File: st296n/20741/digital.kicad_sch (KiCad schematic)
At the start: 61 parts, among them J2 ID, Q14 "1A", U1 8051, U13 74LS155, U2 74LS573, U21 74LS174, U22 74LS174, U23 74LS174, U24 74LS257, U27 74LS00, U28 74LS196, U29 74LS123, U3 74LS14, U30 74F08, U4 CDM6264, U9 11741-502, Y1 10MHz, Y2 20MHz

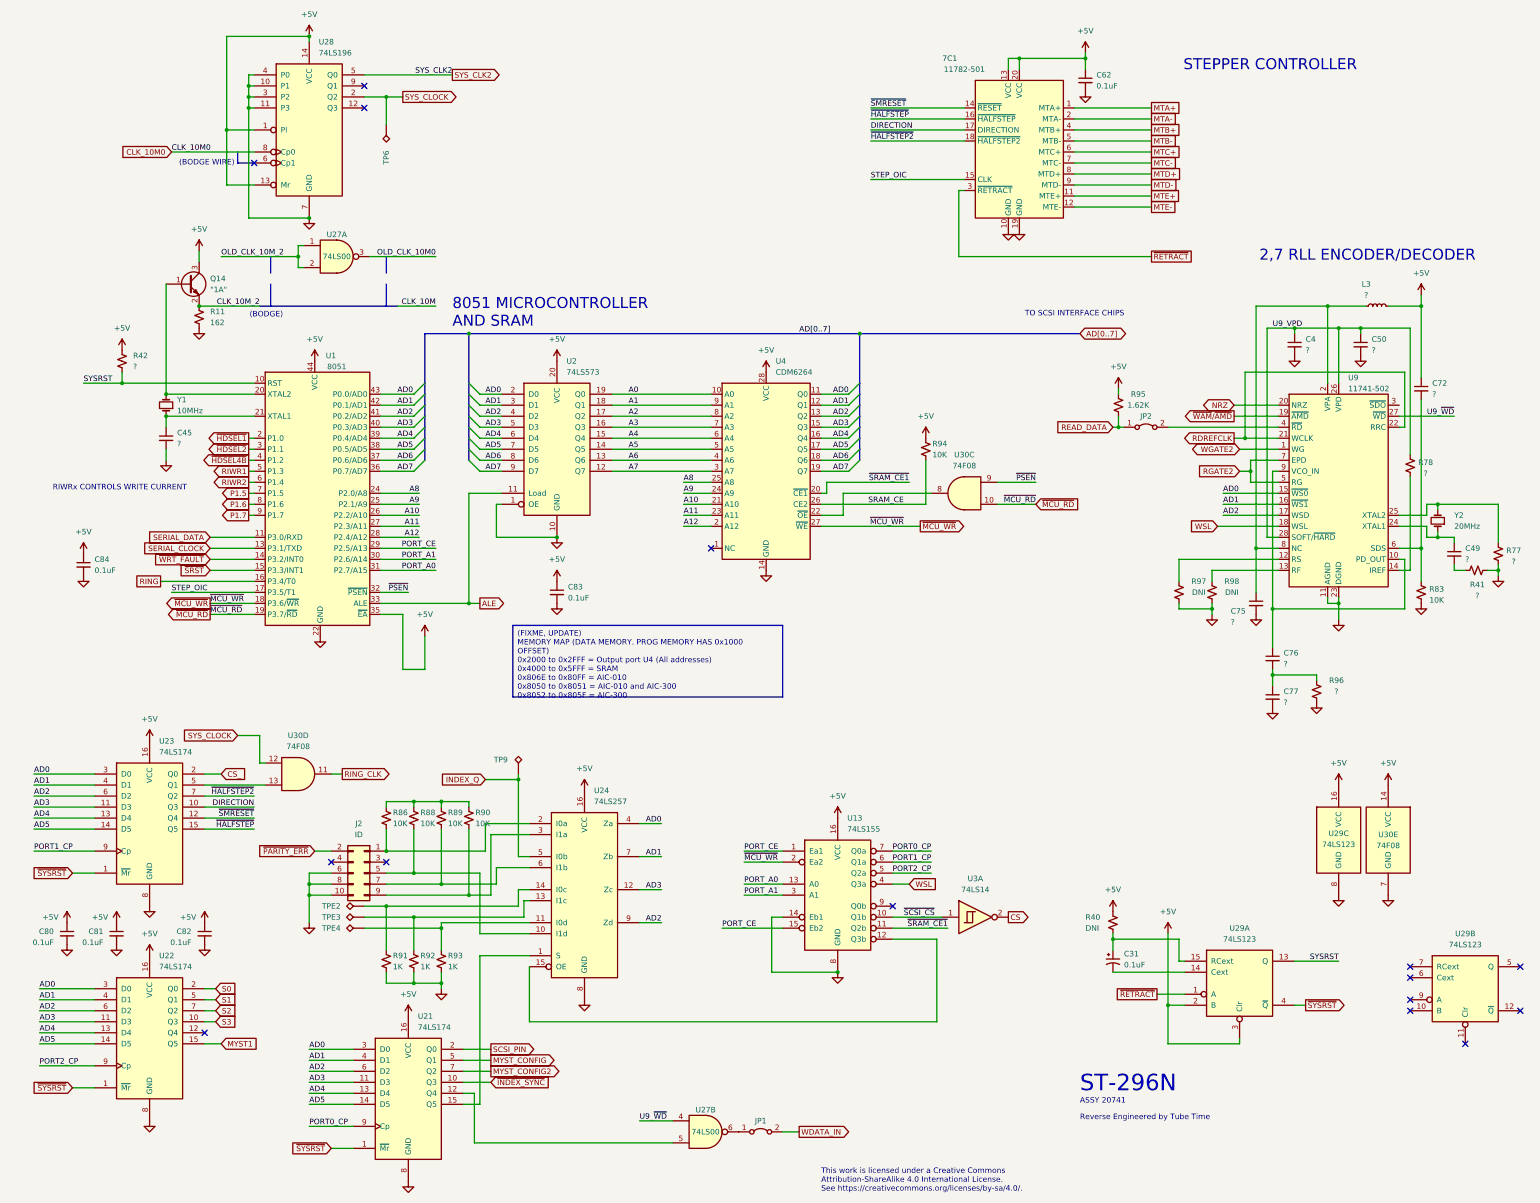
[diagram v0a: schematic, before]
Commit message: st296n fix passives
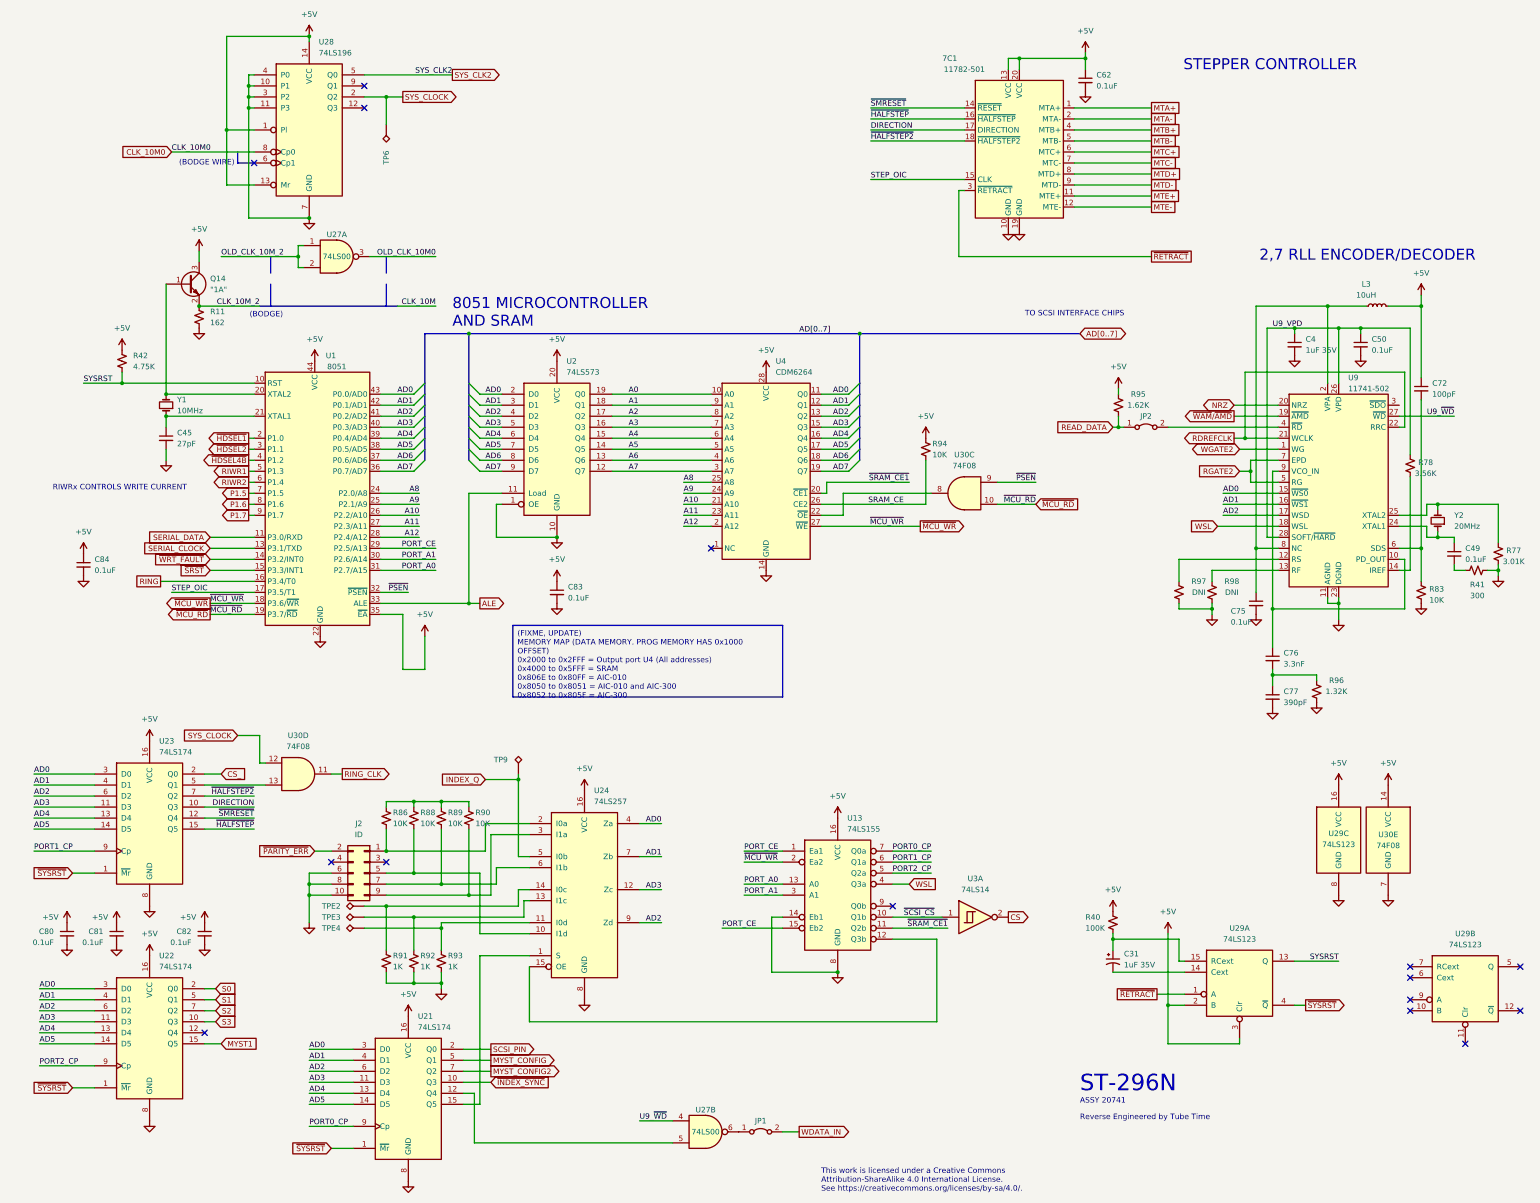
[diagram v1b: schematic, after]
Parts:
- C31: value 0.1uF -> 1uF 35V
- C4: value ? -> 1uF 35V
- C45: value ? -> 27pF
- C49, C50, C75: value ? -> 0.1uF
- C72: value ? -> 100pF
- C76: value ? -> 3.3nF
- C77: value ? -> 390pF
- L3: value ? -> 10uH
- R40: value DNI -> 100K
- R41: value ? -> 300
- R42: value ? -> 4.75K
- R77: value ? -> 3.01K
- R78: value ? -> 3.56K
- R96: value ? -> 1.32K
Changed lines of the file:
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@@
 			)
 		)
-		(property "Value" "?"
+		(property "Value" "4.75K"
 			(at 83.82 92.7099 0)
 			(effects
@@
 		(fields_autoplaced yes)
 		(property "Reference" "C31"
-			(at 312.42 228.1682 0)
+			(at 312.42 228.1681 0)
 			(effects
 				(font
@@
 			)
 		)
-		(property "Value" "0.1uF"
-			(at 312.42 230.7082 0)
+		(property "Value" "1uF 35V"
+			(at 312.42 230.7081 0)
 			(effects
 				(font
@@
 			)
 		)
-		(property "Value" "?"
+		(property "Value" "300"
 			(at 393.954 145.542 90)
 			(effects
@@
 			)
 		)
-		(property "Value" "?"
+		(property "Value" "3.56K"
 			(at 382.016 117.348 0)
 			(effects
@@
 			)
 		)
-		(property "Value" "?"
+		(property "Value" "0.1uF"
 			(at 391.16 137.1662 0)
 			(effects
@@
 			)
 		)
-		(property "Value" "?"
+		(property "Value" "0.1uF"
 			(at 337.058 151.638 0)
 			(effects
@@
 			)
 		)
-		(property "Value" "?"
+		(property "Value" "3.01K"
 			(at 402.336 137.668 0)
 			(effects
@@
 			)
 		)
-		(property "Value" "?"
+		(property "Value" "390pF"
 			(at 349.25 170.1862 0)
 			(effects
@@
 			)
 		)
-		(property "Value" "?"
+		(property "Value" "1.32K"
 			(at 361.442 167.64 0)
 			(effects
@@
 			)
 		)
-		(property "Value" "?"
+		(property "Value" "0.1uF"
 			(at 369.57 88.9062 0)
 			(effects
@@
 			)
 		)
-		(property "Value" "?"
+		(property "Value" "3.3nF"
 			(at 349.25 161.2962 0)
 			(effects
@@
 			)
 		)
-		(property "Value" "?"
+		(property "Value" "100pF"
 			(at 383.54 99.0662 0)
 			(effects
@@
 			)
 		)
-		(property "Value" "?"
+		(property "Value" "10uH"
 			(at 368.3 76.2 90)
 			(effects
@@
 			)
 		)
-		(property "Value" "?"
+		(property "Value" "1uF 35V"
 			(at 354.33 88.9062 0)
 			(effects
@@
 			)
 		)
-		(property "Value" "?"
+		(property "Value" "27pF"
 			(at 93.98 110.4962 0)
 			(effects
@@
 			)
 		)
-		(property "Value" "DNI"
+		(property "Value" "100K"
 			(at 303.53 222.25 0)
 			(effects

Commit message: st296n update symbol with more chip info
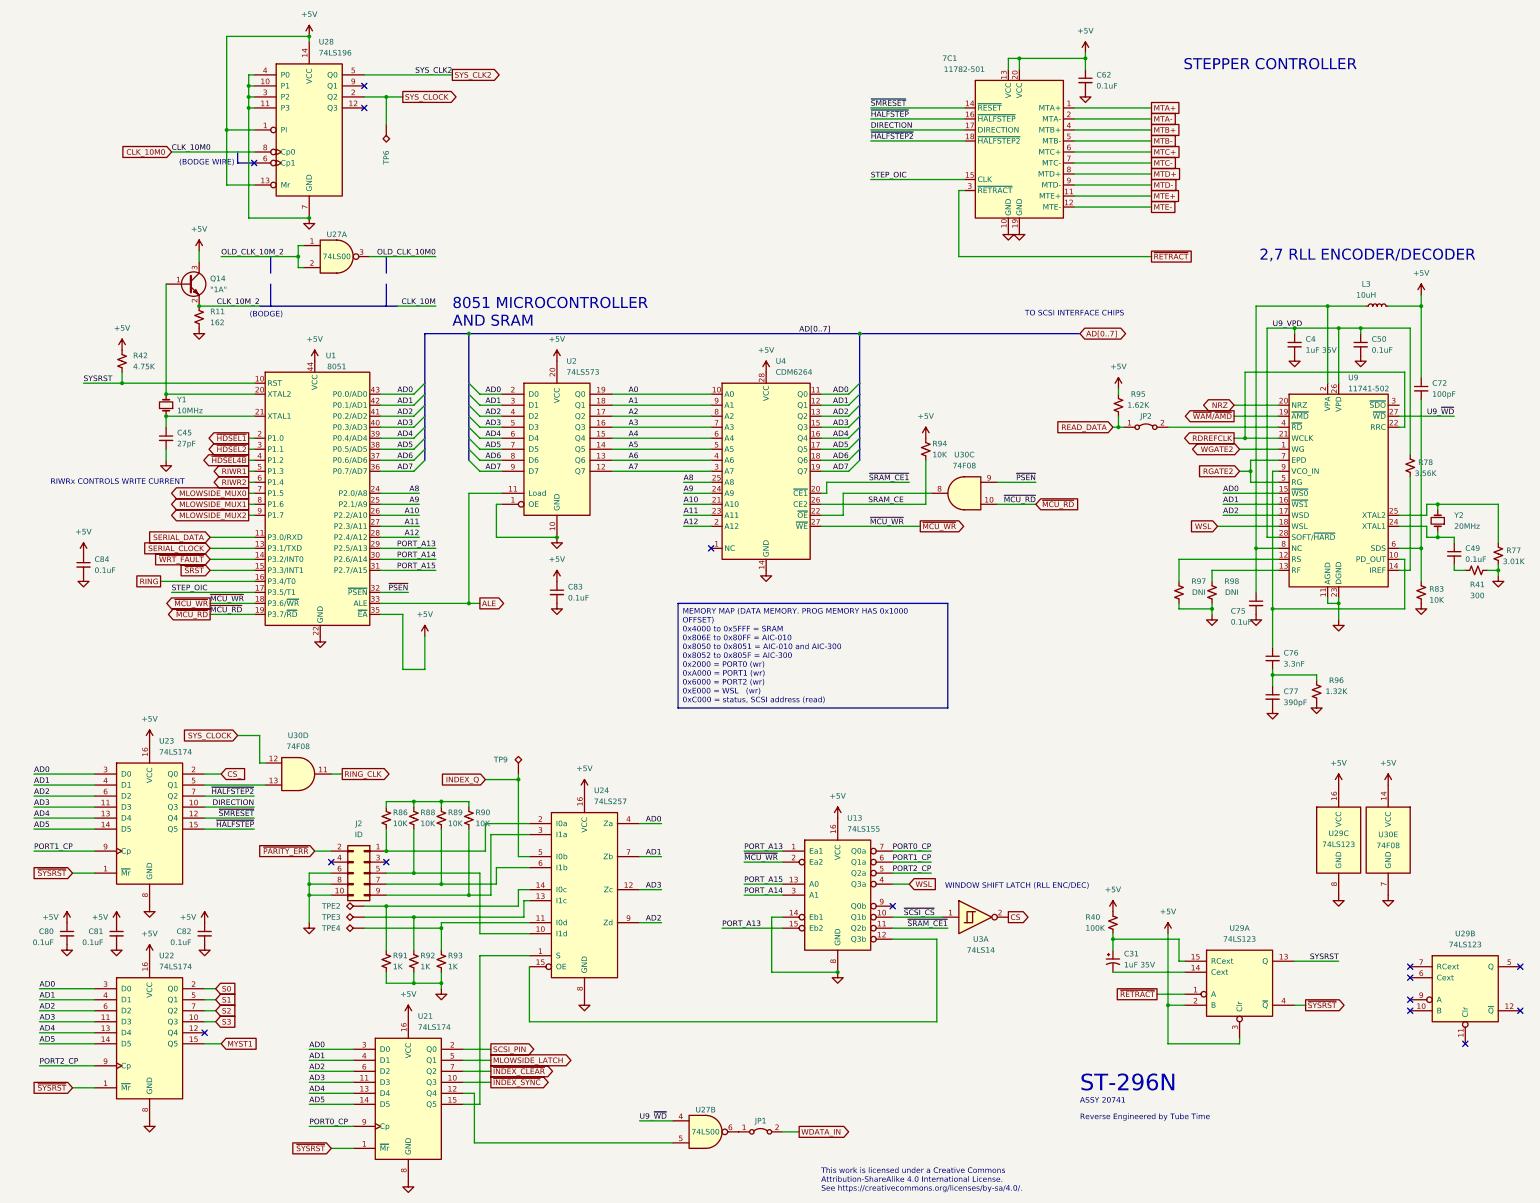
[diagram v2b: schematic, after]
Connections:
- net MYST_CONFIG renamed MLOWSIDE_LATCH
- net MYST_CONFIG2 renamed ~{INDEX_CLEAR}
- net P1.5 renamed MLOWSIDE_MUX0
- net P1.6 renamed MLOWSIDE_MUX1
- net P1.7 renamed MLOWSIDE_MUX2
- net PORT_A0 renamed PORT_A15
- net PORT_A1 renamed PORT_A14
- net PORT_CE renamed PORT_A13
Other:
- note added: "WINDOW SHIFT LATCH (RLL ENC/DEC)"
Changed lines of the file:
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@@
 		)
 	)
-	(text_box "(FIXME, UPDATE)\nMEMORY MAP (DATA MEMORY. PROG MEMORY HAS 0x1000 OFFSET)\n0x2000 to 0x2FFF = Output port U4 (All addresses)\n0x4000 to 0x5FFF = SRAM\n0x806E to 0x80FF = AIC-010\n0x8050 to 0x8051 = AIC-010 and AIC-300\n0x8052 to 0x805F = AIC-300"
+	(text_box "MEMORY MAP (DATA MEMORY. PROG MEMORY HAS 0x1000 OFFSET)\n0x4000 to 0x5FFF = SRAM\n0x806E to 0x80FF = AIC-010\n0x8050 to 0x8051 = AIC-010 and AIC-300\n0x8052 to 0x805F = AIC-300\n0x2000 = PORT0 (wr)\n0xA000 = PORT1 (wr)\n0x6000 = PORT2 (wr)\n0xE000 = WSL   (wr)\n0xC000 = status, SCSI address (read)\n\n"
 		(exclude_from_sim no)
-		(at 171.45 152.4 0)
-		(size 62.23 16.51)
+		(at 209.55 147.32 0)
+		(size 62.23 24.13)
 		(stroke
 			(width 0)
@@
 		)
 	)
+	(text "WINDOW SHIFT LATCH (RLL ENC/DEC)"
+		(exclude_from_sim no)
+		(at 287.782 212.598 0)
+		(effects
+			(font
+				(size 1.27 1.27)
+			)
+		)
+	)
 	(text "8051 MICROCONTROLLER\nAND SRAM"
 		(exclude_from_sim no)
@@
 	(text "RIWRx CONTROLS WRITE CURRENT"
 		(exclude_from_sim no)
-		(at 65.278 121.412 0)
+		(at 64.77 120.142 0)
 		(effects
 			(font
@@
 		)
 	)
-	(label "PORT_CE"
+	(label "PORT_A13"
 		(at 153.67 134.62 180)
 		(fields_autoplaced yes)
@@
 		)
 	)
-	(label "PORT_A0"
+	(label "PORT_A15"
 		(at 153.67 139.7 180)
 		(fields_autoplaced yes)
@@
 		)
 	)
-	(label "PORT_A1"
+	(label "PORT_A14"
 		(at 153.67 137.16 180)
 		(fields_autoplaced yes)
@@
 		)
 	)
-	(label "PORT_CE"
+	(label "PORT_A13"
 		(at 224.79 204.47 0)
 		(fields_autoplaced yes)
@@
 		)
 	)
-	(label "PORT_A0"
+	(label "PORT_A15"
 		(at 224.79 212.09 0)
 		(fields_autoplaced yes)
@@
 		)
 	)
-	(label "PORT_A1"
+	(label "PORT_A14"
 		(at 224.79 214.63 0)
 		(fields_autoplaced yes)
@@
 		)
 	)
-	(label "PORT_CE"
+	(label "PORT_A13"
 		(at 219.71 222.25 0)
 		(fields_autoplaced yes)
@@
 		)
 	)
-	(global_label "P1.6"
+	(global_label "MLOWSIDE_MUX1"
 		(shape output)
 		(at 110.49 124.46 180)
@@
 		)
 	)
-	(global_label "P1.7"
+	(global_label "MLOWSIDE_MUX2"
 		(shape output)
 		(at 110.49 127 180)
@@
 		)
 	)
-	(global_label "MYST_CONFIG2"
+	(global_label "~{INDEX_CLEAR}"
 		(shape output)
 		(at 166.37 255.27 0)
@@
 		)
 	)
-	(global_label "MYST_CONFIG"
+	(global_label "MLOWSIDE_LATCH"
 		(shape output)
 		(at 166.37 252.73 0)
@@
 	)
 	(global_label "~{INDEX_SYNC}"
-		(shape input)
+		(shape output)
 		(at 166.37 257.81 0)
 		(fields_autoplaced yes)
@@
 		)
 	)
-	(global_label "P1.5"
+	(global_label "MLOWSIDE_MUX0"
 		(shape output)
 		(at 110.49 121.92 180)
@@
 		(on_board yes)
 		(dnp no)
-		(fields_autoplaced yes)
 		(property "Reference" "U3"
-			(at 278.13 210.82 0)
+			(at 279.4 224.79 0)
 			(effects
 				(font
@@
 		)
 		(property "Value" "74LS14"
-			(at 278.13 213.36 0)
+			(at 279.4 227.33 0)
 			(effects
 				(font
